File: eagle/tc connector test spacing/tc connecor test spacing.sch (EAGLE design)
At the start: 31 parts

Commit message: Inside and outside draft versions chosen.
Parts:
- removed U$1, U$10, U$11, U$12, U$15, U$16, U$17, U$18, U$19, U$2, U$20, U$21, U$22, U$23, U$24, U$27, U$28, U$3, U$4, U$5, U$6, U$7, U$8, U$9: TC-MINI-SINGLE, PaxInstruments-Connectors:TC-MINI-SINGLE
- removed U$29, U$30: POGO-2.54-2P, PaxInstruments-Connectors:POGO-2.54-2P
- removed U$31: POGO-2.54-6P, PaxInstruments-Connectors:POGO-2.54-6P
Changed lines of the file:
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@@
 </classes>
 <parts>
-<part name="U$1" library="PaxInstruments-Connectors" deviceset="TC-MINI-SINGLE" device=""/>
-<part name="U$2" library="PaxInstruments-Connectors" deviceset="TC-MINI-SINGLE" device=""/>
-<part name="U$3" library="PaxInstruments-Connectors" deviceset="TC-MINI-SINGLE" device=""/>
-<part name="U$4" library="PaxInstruments-Connectors" deviceset="TC-MINI-SINGLE" device=""/>
-<part name="U$5" library="PaxInstruments-Connectors" deviceset="TC-MINI-SINGLE" device=""/>
-<part name="U$6" library="PaxInstruments-Connectors" deviceset="TC-MINI-SINGLE" device=""/>
-<part name="U$7" library="PaxInstruments-Connectors" deviceset="TC-MINI-SINGLE" device=""/>
-<part name="U$8" library="PaxInstruments-Connectors" deviceset="TC-MINI-SINGLE" device=""/>
-<part name="U$9" library="PaxInstruments-Connectors" deviceset="TC-MINI-SINGLE" device=""/>
-<part name="U$10" library="PaxInstruments-Connectors" deviceset="TC-MINI-SINGLE" device=""/>
-<part name="U$11" library="PaxInstruments-Connectors" deviceset="TC-MINI-SINGLE" device=""/>
-<part name="U$12" library="PaxInstruments-Connectors" deviceset="TC-MINI-SINGLE" device=""/>
 <part name="U$13" library="PaxInstruments-Connectors" deviceset="TC-MINI-SINGLE" device=""/>
 <part name="U$14" library="PaxInstruments-Connectors" deviceset="TC-MINI-SINGLE" device=""/>
-<part name="U$15" library="PaxInstruments-Connectors" deviceset="TC-MINI-SINGLE" device=""/>
-<part name="U$16" library="PaxInstruments-Connectors" deviceset="TC-MINI-SINGLE" device=""/>
-<part name="U$17" library="PaxInstruments-Connectors" deviceset="TC-MINI-SINGLE" device=""/>
-<part name="U$18" library="PaxInstruments-Connectors" deviceset="TC-MINI-SINGLE" device=""/>
-<part name="U$19" library="PaxInstruments-Connectors" deviceset="TC-MINI-SINGLE" device=""/>
-<part name="U$20" library="PaxInstruments-Connectors" deviceset="TC-MINI-SINGLE" device=""/>
-<part name="U$21" library="PaxInstruments-Connectors" deviceset="TC-MINI-SINGLE" device=""/>
-<part name="U$22" library="PaxInstruments-Connectors" deviceset="TC-MINI-SINGLE" device=""/>
-<part name="U$23" library="PaxInstruments-Connectors" deviceset="TC-MINI-SINGLE" device=""/>
-<part name="U$24" library="PaxInstruments-Connectors" deviceset="TC-MINI-SINGLE" device=""/>
 <part name="U$25" library="PaxInstruments-Connectors" deviceset="TC-MINI-SINGLE" device=""/>
 <part name="U$26" library="PaxInstruments-Connectors" deviceset="TC-MINI-SINGLE" device=""/>
-<part name="U$27" library="PaxInstruments-Connectors" deviceset="TC-MINI-SINGLE" device=""/>
-<part name="U$28" library="PaxInstruments-Connectors" deviceset="TC-MINI-SINGLE" device=""/>
-<part name="U$29" library="PaxInstruments-Connectors" deviceset="POGO-2.54-2P" device=""/>
-<part name="U$30" library="PaxInstruments-Connectors" deviceset="POGO-2.54-2P" device=""/>
-<part name="U$31" library="PaxInstruments-Connectors" deviceset="POGO-2.54-6P" device=""/>
 </parts>
 <sheets>
@@
 </plain>
 <instances>
-<instance part="U$1" gate="G$1" x="22.86" y="71.12"/>
-<instance part="U$2" gate="G$1" x="22.86" y="66.04"/>
-<instance part="U$3" gate="G$1" x="22.86" y="60.96"/>
-<instance part="U$4" gate="G$1" x="22.86" y="55.88"/>
-<instance part="U$5" gate="G$1" x="35.56" y="71.12"/>
-<instance part="U$6" gate="G$1" x="35.56" y="66.04"/>
-<instance part="U$7" gate="G$1" x="35.56" y="60.96"/>
-<instance part="U$8" gate="G$1" x="35.56" y="55.88"/>
-<instance part="U$9" gate="G$1" x="48.26" y="71.12"/>
-<instance part="U$10" gate="G$1" x="48.26" y="66.04"/>
-<instance part="U$11" gate="G$1" x="48.26" y="60.96"/>
-<instance part="U$12" gate="G$1" x="48.26" y="55.88"/>
 <instance part="U$13" gate="G$1" x="22.86" y="50.8"/>
 <instance part="U$14" gate="G$1" x="22.86" y="45.72"/>
-<instance part="U$15" gate="G$1" x="22.86" y="40.64"/>
-<instance part="U$16" gate="G$1" x="22.86" y="35.56"/>
-<instance part="U$17" gate="G$1" x="35.56" y="50.8"/>
-<instance part="U$18" gate="G$1" x="35.56" y="45.72"/>
-<instance part="U$19" gate="G$1" x="35.56" y="40.64"/>
-<instance part="U$20" gate="G$1" x="35.56" y="35.56"/>
-<instance part="U$21" gate="G$1" x="48.26" y="50.8"/>
-<instance part="U$22" gate="G$1" x="48.26" y="45.72"/>
-<instance part="U$23" gate="G$1" x="48.26" y="40.64"/>
-<instance part="U$24" gate="G$1" x="48.26" y="35.56"/>
 <instance part="U$25" gate="G$1" x="22.86" y="30.48"/>
 <instance part="U$26" gate="G$1" x="22.86" y="25.4"/>
-<instance part="U$27" gate="G$1" x="35.56" y="30.48"/>
-<instance part="U$28" gate="G$1" x="35.56" y="25.4"/>
-<instance part="U$29" gate="G$1" x="66.04" y="73.66"/>
-<instance part="U$29" gate="G$2" x="71.12" y="73.66"/>
-<instance part="U$30" gate="G$1" x="76.2" y="73.66"/>
-<instance part="U$31" gate="G$1" x="66.04" y="60.96"/>
-<instance part="U$31" gate="G$2" x="71.12" y="60.96"/>
-<instance part="U$31" gate="G$3" x="76.2" y="60.96"/>
 </instances>
 <busses>

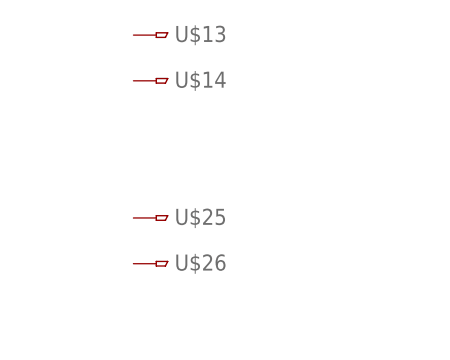
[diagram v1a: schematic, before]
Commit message: This could be the production footprint.:
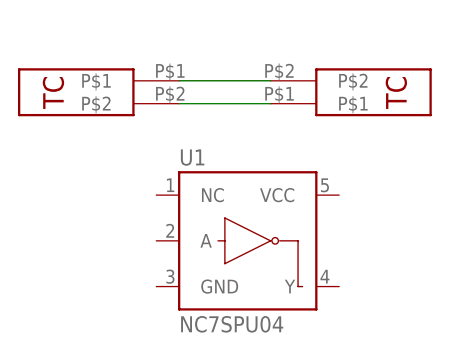
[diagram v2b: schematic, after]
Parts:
- removed U$13, U$14, U$25, U$26: TC-MINI-SINGLE, PaxInstruments-Connectors:TC-MINI-SINGLE
- added U$1: TC-MINI-INSIDE, PaxInstruments-Connectors:TC-MINI-INSIDE
- added U$2: TC-MINI-OUTSIDE, PaxInstruments-Connectors:TC-MINI-OUTSIDE
- added U1: NC7SPU04, SparkFun-DigitalIC:INVERTER_SC70-5
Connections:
- new net N$1: U$1.P$1, U$2.P$2
- new net N$2: U$1.P$2, U$2.P$1
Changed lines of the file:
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@@
 <layer number="54" name="bGND_GNDA" color="7" fill="1" visible="no" active="no"/>
 <layer number="56" name="wert" color="7" fill="1" visible="no" active="no"/>
+<layer number="57" name="tCAD" color="7" fill="1" visible="no" active="no"/>
+<layer number="59" name="tCarbon" color="7" fill="1" visible="no" active="no"/>
+<layer number="60" name="bCarbon" color="7" fill="1" visible="no" active="no"/>
+<layer number="90" name="Modules" color="5" fill="1" visible="yes" active="yes"/>
 <layer number="91" name="Nets" color="2" fill="1" visible="yes" active="yes"/>
 <layer number="92" name="Busses" color="1" fill="1" visible="yes" active="yes"/>
@@
 <layer number="127" name="_tValues" color="7" fill="1" visible="yes" active="yes"/>
 <layer number="128" name="_bValues" color="7" fill="1" visible="yes" active="yes"/>
+<layer number="129" name="Mask" color="7" fill="1" visible="yes" active="yes"/>
 <layer number="131" name="tAdjust" color="7" fill="1" visible="yes" active="yes"/>
 <layer number="132" name="bAdjust" color="7" fill="1" visible="yes" active="yes"/>
 <layer number="144" name="Drill_legend" color="7" fill="1" visible="yes" active="yes"/>
+<layer number="150" name="Notes" color="7" fill="1" visible="yes" active="yes"/>
 <layer number="151" name="HeatSink" color="7" fill="1" visible="yes" active="yes"/>
 <layer number="152" name="_bDocu" color="7" fill="1" visible="yes" active="yes"/>
+<layer number="153" name="FabDoc1" color="7" fill="1" visible="yes" active="yes"/>
+<layer number="154" name="FabDoc2" color="7" fill="1" visible="yes" active="yes"/>
+<layer number="155" name="FabDoc3" color="7" fill="1" visible="yes" active="yes"/>
 <layer number="199" name="Contour" color="7" fill="1" visible="yes" active="yes"/>
 <layer number="200" name="200bmp" color="7" fill="1" visible="yes" active="yes"/>
@@
 <layer number="223" name="223bmp" color="7" fill="1" visible="yes" active="yes"/>
 <layer number="224" name="224bmp" color="7" fill="1" visible="yes" active="yes"/>
+<layer number="225" name="225bmp" color="7" fill="1" visible="yes" active="yes"/>
+<layer number="226" name="226bmp" color="7" fill="1" visible="yes" active="yes"/>
+<layer number="227" name="227bmp" color="7" fill="1" visible="yes" active="yes"/>
+<layer number="228" name="228bmp" color="7" fill="1" visible="yes" active="yes"/>
+<layer number="229" name="229bmp" color="7" fill="1" visible="yes" active="yes"/>
+<layer number="230" name="230bmp" color="7" fill="1" visible="yes" active="yes"/>
 <layer number="231" name="Eagle3D_PG1" color="7" fill="1" visible="yes" active="yes"/>
 <layer number="232" name="Eagle3D_PG2" color="7" fill="1" visible="yes" active="yes"/>
@@
 <layer number="251" name="SMDround" color="7" fill="1" visible="yes" active="yes"/>
 <layer number="254" name="cooling" color="7" fill="1" visible="yes" active="yes"/>
+<layer number="255" name="routoute" color="7" fill="1" visible="yes" active="yes"/>
 </layers>
 <schematic xreflabel="%F%N/%S.%C%R" xrefpart="/%S.%C%R">
@@
 </classes>
 <parts>
-<part name="U$13" library="PaxInstruments-Connectors" deviceset="TC-MINI-SINGLE" device=""/>
-<part name="U$14" library="PaxInstruments-Connectors" deviceset="TC-MINI-SINGLE" device=""/>
-<part name="U$25" library="PaxInstruments-Connectors" deviceset="TC-MINI-SINGLE" device=""/>
-<part name="U$26" library="PaxInstruments-Connectors" deviceset="TC-MINI-SINGLE" device=""/>
+<part name="U$1" library="PaxInstruments-Connectors" deviceset="TC-MINI-INSIDE" device=""/>
+<part name="U$2" library="PaxInstruments-Connectors" deviceset="TC-MINI-OUTSIDE" device=""/>
+<part name="U1" library="SparkFun-DigitalIC" deviceset="INVERTER" device="_SC70-5" value="NC7SPU04"/>
 </parts>
 <sheets>
@@
 </plain>
 <instances>
-<instance part="U$13" gate="G$1" x="22.86" y="50.8"/>
-<instance part="U$14" gate="G$1" x="22.86" y="45.72"/>
-<instance part="U$25" gate="G$1" x="22.86" y="30.48"/>
-<instance part="U$26" gate="G$1" x="22.86" y="25.4"/>
+<instance part="U$1" gate="G$1" x="20.32" y="45.72"/>
+<instance part="U$2" gate="G$1" x="40.64" y="43.18" rot="R180"/>
+<instance part="U1" gate="G$1" x="33.02" y="27.94"/>
 </instances>
 <busses>
 </busses>
 <nets>
+<net name="N$1" class="0">
+<segment>
+<pinref part="U$1" gate="G$1" pin="P$1"/>
+<pinref part="U$2" gate="G$1" pin="P$2"/>
+<wire x1="25.4" y1="45.72" x2="35.56" y2="45.72" width="0.1524" layer="91"/>
+</segment>
+</net>
+<net name="N$2" class="0">
+<segment>
+<pinref part="U$1" gate="G$1" pin="P$2"/>
+<pinref part="U$2" gate="G$1" pin="P$1"/>
+<wire x1="25.4" y1="43.18" x2="35.56" y2="43.18" width="0.1524" layer="91"/>
+</segment>
+</net>
 </nets>
 </sheet>
